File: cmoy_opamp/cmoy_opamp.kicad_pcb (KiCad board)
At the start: 2 copper layers, 89.7 x 67.6 mm, 57 parts, among them J1 AudioJack3, J2 AudioJack3, SW1 SPST, U1 MC33178, U2 LMH6642, U3 LMH6642, U4 LMH6642

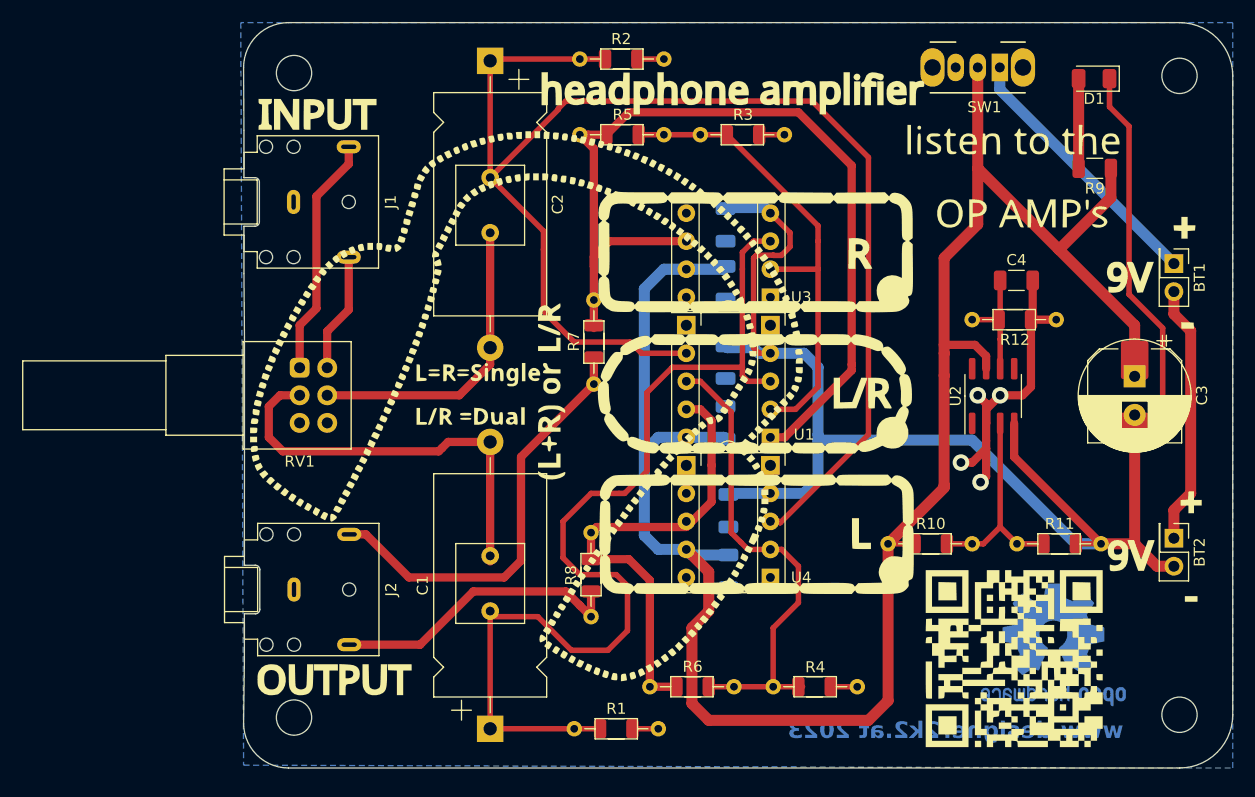
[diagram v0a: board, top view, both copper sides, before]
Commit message: Bugfix ZIF socket against R3/4/5/6
Moving R3/3/4/5/6 a bit to the outside to have clearance for the ZIF socket.
Like this the ZIF socket can sit flush and does not need to be stacked on DIL socket´s.
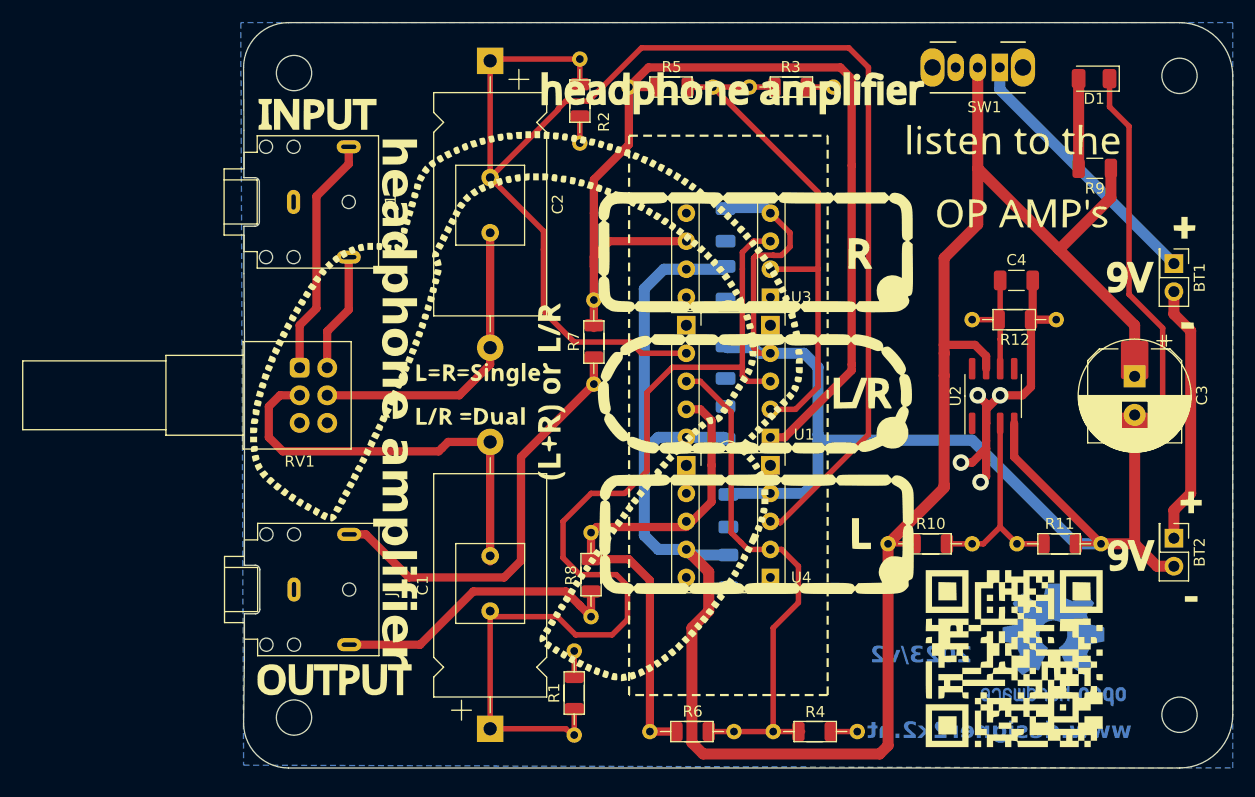
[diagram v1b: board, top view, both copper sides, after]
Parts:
- moved R3_1 6.20 mm to (195.2, 49.0)
- moved R5 6.20 mm to (188.1, 49.0)
- moved R5_1 6.20 mm to (184.3, 49.0)
- moved R3 6.11 mm to (198.9, 49.0)
- moved R2 5.30 mm to (179.8, 50.2), turned to -90 degrees
- moved R1 5.00 mm to (179.3, 103.9), turned to 90 degrees
- moved R4 4.06 mm to (201.1, 107.4)
- moved R4_1 4.06 mm to (205.0, 107.4)
- moved R6 4.06 mm to (190.1, 107.4)
- moved R6_1 4.06 mm to (186.2, 107.4)
- moved R1_1 0.57 mm to (179.3, 107.8), turned to 90 degrees
- turned R2_1 to -90 degrees
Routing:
- net /1O: track 83.8 -> 93.1 mm
- net /2+: track 126.3 -> 135.1 mm
- net V+: track 184.5 -> 191.5 mm
- net /1-: track 43.8 -> 48.6 mm
- net /2O: track 42.7 -> 46.8 mm
- net /2-: track 43.9 -> 47.9 mm
- net /1+: track 91.9 -> 90.4 mm
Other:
- board text added: "2023/v2"
- board text added: "Use either 1 dual Op Amp in the center, or 2 single Op Amp´s on the outside positon."
- board text added: "headphone amplifier"
- board text added: "www.designer2k2.at"
- board text removed: "www.designer2k2.at 2023"

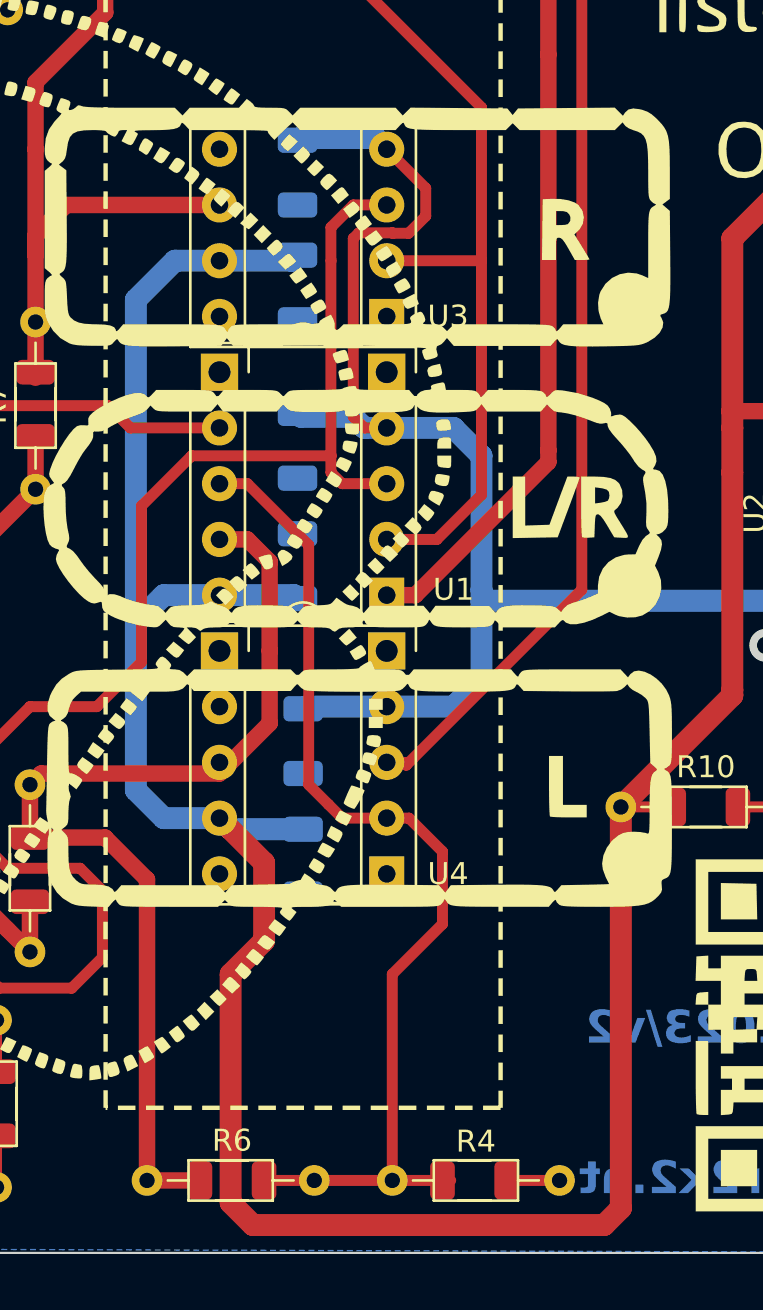
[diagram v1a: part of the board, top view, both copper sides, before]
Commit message: change drilling to fit zif socket
0,8mm increased to 1,1mm to fit the 0,9mm ZIF socket pins
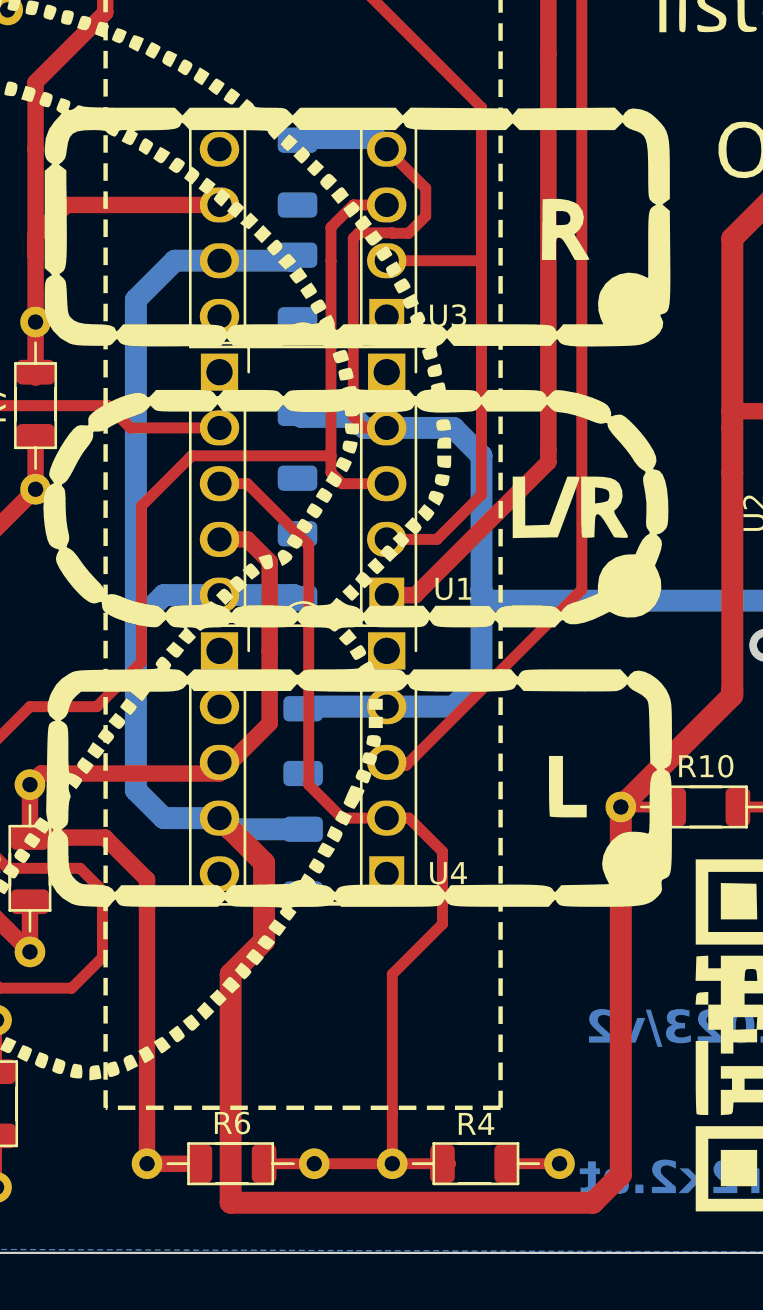
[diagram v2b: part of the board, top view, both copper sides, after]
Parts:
- U1: value MC33178 -> OPA2227
- U3, U4: value LMH6642 -> OPA134
- moved R4 0.76 mm to (201.1, 106.7)
- moved R4_1 0.76 mm to (205.0, 106.7)
- moved R6 0.76 mm to (190.1, 106.7)
- moved R6_1 0.76 mm to (186.2, 106.7)
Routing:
- net V+: track 191.5 -> 189.8 mm
- net /2O: track 46.8 -> 46.0 mm
- net /2-: track 47.9 -> 47.2 mm

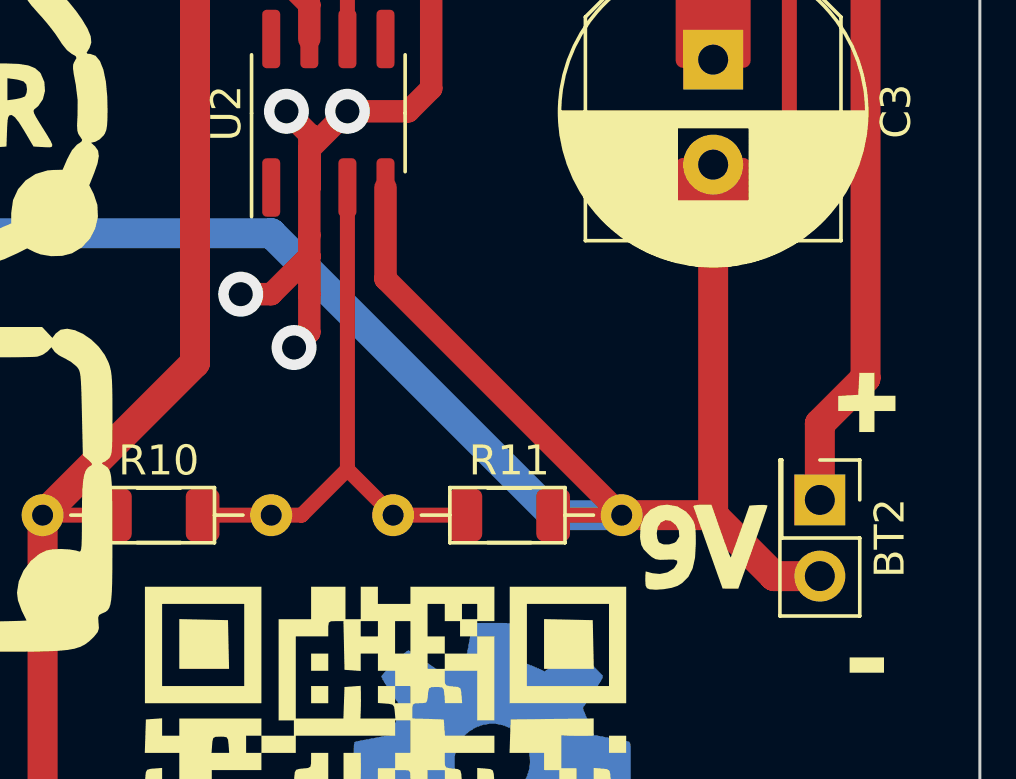
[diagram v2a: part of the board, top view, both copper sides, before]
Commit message: Add TLE2426 as option
TLE2426 option alternative to R10/R11 voltage divider
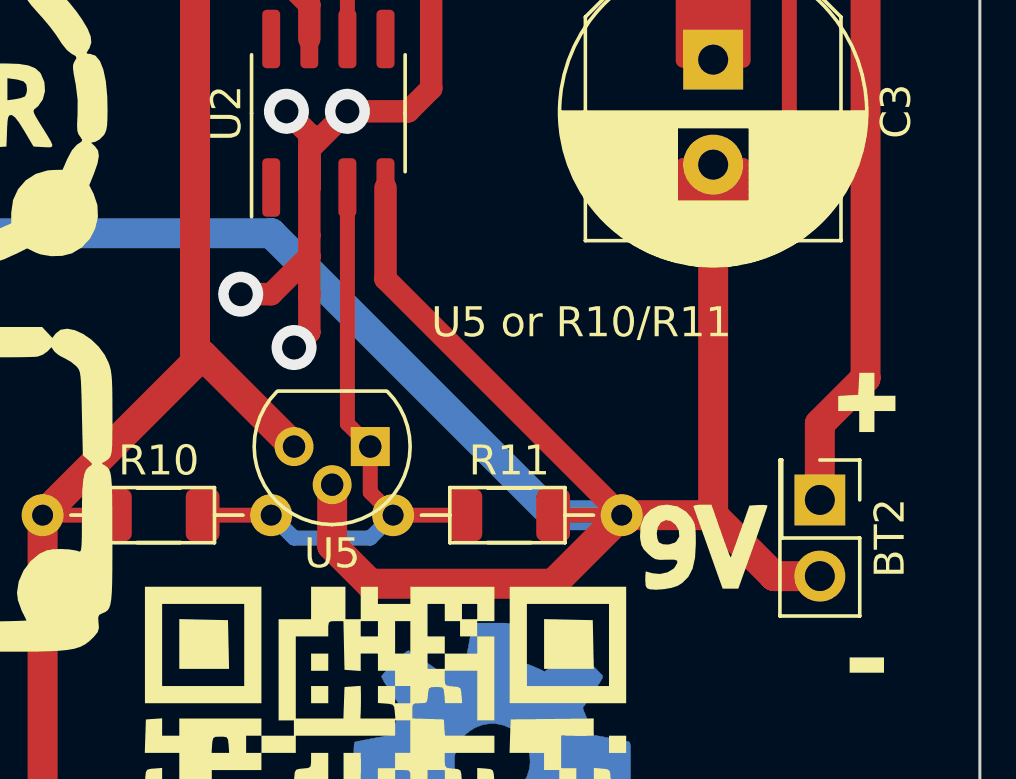
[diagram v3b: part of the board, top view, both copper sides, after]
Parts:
- added U5: TLE2426xLP, Package_TO_SOT_THT:TO-92, F.Cu at (218.7, 88.1)
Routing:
- net V-: track 151.0 -> 164.2 mm
- net V+: track 189.8 -> 194.3 mm
- net Net-(U2-+): track 19.4 -> 20.9 mm
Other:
- board text added: "U5 or R10/R11"
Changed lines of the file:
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@@
+    )
+  )
+  (footprint "Package_TO_SOT_THT:TO-92" (layer "F.Cu")
+    (at 218.694 88.138 180)
+    (descr "TO-92 leads molded, narrow, drill 0.75mm (see NXP sot054_po.pdf)")
+    (tags "to-92 sc-43 sc-43a sot54 PA33 transistor")
+    (property "Sheetfile" "cmoy_opamp.kicad_sch")
+    (property "Sheetname" "")
+    (property "ki_description" "Precision virtual ground, 4V to 40V input, TO-92")
+    (property "ki_keywords" "Rail splitter precision virtual ground")
+    (attr through_hole)
+    (fp_text reference "U5" (at 1.27 -3.56) (layer "F.SilkS")
+        (effects (font (size 1 1) (thickness 0.15)))
+    )
+    (fp_text value "TLE2426xLP" (at 1.27 2.79) (layer "F.Fab")
+        (effects (font (size 1 1) (thickness 0.15)))
+    )
+    (fp_text user "${REFERENCE}" (at 1.27 0) (layer "F.Fab")
+        (effects (font (size 1 1) (thickness 0.15)))
+    )
+    (fp_line (start -0.53 1.85) (end 3.07 1.85)
+      (stroke (width 0.12) (type solid)) (layer "F.SilkS"))
+    (fp_arc (start -0.568478 1.838478) (mid -1.132087 -0.994977) (end 1.27 -2.6)
+      (stroke (width 0.12) (type solid)) (layer "F.SilkS"))
+    (fp_arc (start 1.27 -2.6) (mid 3.672087 -0.994977) (end 3.108478 1.838478)
+      (stroke (width 0.12) (type solid)) (layer "F.SilkS"))
+    (fp_line (start -1.46 -2.73) (end -1.46 2.01)
+      (stroke (width 0.05) (type solid)) (layer "F.CrtYd"))
+    (fp_line (start -1.46 -2.73) (end 4 -2.73)
+      (stroke (width 0.05) (type solid)) (layer "F.CrtYd"))
+    (fp_line (start 4 2.01) (end -1.46 2.01)
+      (stroke (width 0.05) (type solid)) (layer "F.CrtYd"))
+    (fp_line (start 4 2.01) (end 4 -2.73)
+      (stroke (width 0.05) (type solid)) (layer "F.CrtYd"))
+    (fp_line (start -0.5 1.75) (end 3 1.75)
+      (stroke (width 0.1) (type solid)) (layer "F.Fab"))
+    (fp_arc (start -0.483625 1.753625) (mid -1.021221 -0.949055) (end 1.27 -2.48)
+      (stroke (width 0.1) (type solid)) (layer "F.Fab"))
+    (fp_arc (start 1.27 -2.48) (mid 3.561221 -0.949055) (end 3.023625 1.753625)
+      (stroke (width 0.1) (type solid)) (layer "F.Fab"))
+    (pad "1" thru_hole rect (at 0 0 180) (size 1.3 1.3) (drill 0.75) (layers "*.Cu" "*.Mask")
+      (net 20 "Net-(U2-+)") (pinfunction "OUT") (pintype "power_out"))
+    (pad "2" thru_hole circle (at 1.27 -1.27 180) (size 1.3 1.3) (drill 0.75) (layers "*.Cu" "*.Mask")
+      (net 3 "V-") (pinfunction "COMMON") (pintype "power_in"))
+    (pad "3" thru_hole circle (at 2.54 0 180) (size 1.3 1.3) (drill 0.75) (layers "*.Cu" "*.Mask")
+      (net 8 "V+") (pinfunction "IN") (pintype "power_in"))
+    (model "${KICAD6_3DMODEL_DIR}/Package_TO_SOT_THT.3dshapes/TO-92.wrl"
+      (offset (xyz 0 0 0))
+      (scale (xyz 1 1 1))
+      (rotate (xyz 0 0 0))
     )
   )
@@
     (effects (font (size 3 3) (thickness 0.5) bold) (justify left bottom))
   )
+  (gr_text "U5 or R10/R11" (at 220.726 84.582) (layer "F.SilkS")
+    (effects (font (size 1 1) (thickness 0.15)) (justify left bottom))
+  )
   (segment (start 217.9 49.244) (end 217.9 47.244) (width 1) (layer "B.Cu") (net 1))
   (segment (start 233.68 65.024) (end 217.9 49.244) (width 1) (layer "B.Cu") (net 1))
@@
   (segment (start 235.204 85.852) (end 233.68 87.376) (width 1) (layer "F.Cu") (net 2))
   (segment (start 232.156 92.456) (end 230.124 90.424) (width 1) (layer "F.Cu") (net 3))
+  (segment (start 217.424 89.408) (end 217.424 91.44) (width 1) (layer "F.Cu") (net 3))
   (segment (start 198.882 62.23) (end 197.104 60.452) (width 0.5) (layer "F.Cu") (net 3))
   (segment (start 198.1 64.282) (end 197.378 64.282) (width 0.5) (layer "F.Cu") (net 3))
@@
   (segment (start 230.124 90.424) (end 230.124 81.788) (width 1) (layer "F.Cu") (net 3))
   (segment (start 232.664 70.866) (end 229.616 67.818) (width 0.5) (layer "F.Cu") (net 3))
+  (segment (start 227.076 90.424) (end 224.79 92.71) (width 1) (layer "F.Cu") (net 3))
   (segment (start 219.202 79.502) (end 219.202 82.55) (width 0.75) (layer "F.Cu") (net 3))
   (segment (start 197.378 64.282) (end 197.358 64.262) (width 0.5) (layer "F.Cu") (net 3))
   (segment (start 230.124 81.788) (end 232.664 79.248) (width 0.5) (layer "F.Cu") (net 3))
+  (segment (start 224.79 92.71) (end 218.694 92.71) (width 1) (layer "F.Cu") (net 3))
   (segment (start 197.104 73.152) (end 196.088 73.152) (width 0.5) (layer "F.Cu") (net 3))
+  (segment (start 217.424 91.44) (end 218.694 92.71) (width 1) (layer "F.Cu") (net 3))
   (segment (start 229.616 67.818) (end 229.616 52.578) (width 0.5) (layer "F.Cu") (net 3))
   (segment (start 227.844 48.26) (end 227.844 50.806) (width 0.5) (layer "F.Cu") (net 3))
@@
   (segment (start 206.502 108.458) (end 207.772 107.188) (width 1) (layer "F.Cu") (net 8))
   (segment (start 212.852 64.516) (end 215.9 61.468) (width 1) (layer "F.Cu") (net 8))
+  (segment (start 213.106 85.09) (end 216.154 88.138) (width 1) (layer "F.Cu") (net 8))
   (segment (start 212.852 85.221) (end 212.852 85.09) (width 0.5) (layer "F.Cu") (net 8))
   (segment (start 215.9 56.388) (end 223.266 63.754) (width 1) (layer "F.Cu") (net 8))
@@
   (segment (start 189.992 108.458) (end 206.502 108.458) (width 1) (layer "F.Cu") (net 8))
   (segment (start 189.992 98.044) (end 189.992 108.458) (width 1) (layer "F.Cu") (net 8))
+  (segment (start 212.852 85.09) (end 213.106 85.09) (width 1) (layer "F.Cu") (net 8))
   (segment (start 230.124 70.612) (end 230.124 75.288) (width 1) (layer "F.Cu") (net 8))
   (segment (start 191.516 96.52) (end 189.992 98.044) (width 1) (layer "F.Cu") (net 8))
@@
   (segment (start 191.77 83.312) (end 191.77 79.248) (width 0.75) (layer "F.Cu") (net 19))
   (segment (start 181.356 88.9) (end 180.848 89.408) (width 0.75) (layer "F.Cu") (net 19))
+  (segment (start 217.932 87.376) (end 218.694 88.138) (width 0.5) (layer "F.Cu") (net 20))
+  (segment (start 218.694 88.138) (end 218.694 89.662) (width 0.5) (layer "F.Cu") (net 20))
   (segment (start 219.456 90.424) (end 221.865 90.424) (width 0.5) (layer "F.Cu") (net 20))
-  (segment (start 217.932 88.9) (end 219.456 90.424) (width 0.5) (layer "F.Cu") (net 20))
+  (segment (start 218.694 89.662) (end 219.456 90.424) (width 0.5) (layer "F.Cu") (net 20))
   (segment (start 215.392 90.424) (end 213.106 90.424) (width 0.5) (layer "F.Cu") (net 20))
-  (segment (start 217.932 88.9) (end 216.408 90.424) (width 0.5) (layer "F.Cu") (net 20))
-  (segment (start 216.408 90.424) (end 215.392 90.424) (width 0.5) (layer "F.Cu") (net 20))
-  (segment (start 217.932 79.502) (end 217.932 88.9) (width 0.5) (layer "F.Cu") (net 20))
+  (segment (start 217.932 79.502) (end 217.932 87.376) (width 0.5) (layer "F.Cu") (net 20))
+  (segment (start 216.154 91.186) (end 215.392 90.424) (width 0.5) (layer "B.Cu") (net 20))
+  (segment (start 218.694 91.186) (end 216.154 91.186) (width 0.5) (layer "B.Cu") (net 20))
+  (segment (start 219.456 90.424) (end 218.694 91.186) (width 0.5) (layer "B.Cu") (net 20))
   (zone (net 10) (net_name "GND") (layer "B.Cu") (hatch edge 0.5)
     (connect_pads (clearance 0.3))
